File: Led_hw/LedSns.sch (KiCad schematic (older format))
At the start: 10 parts, among them Q1 TSOP48xx

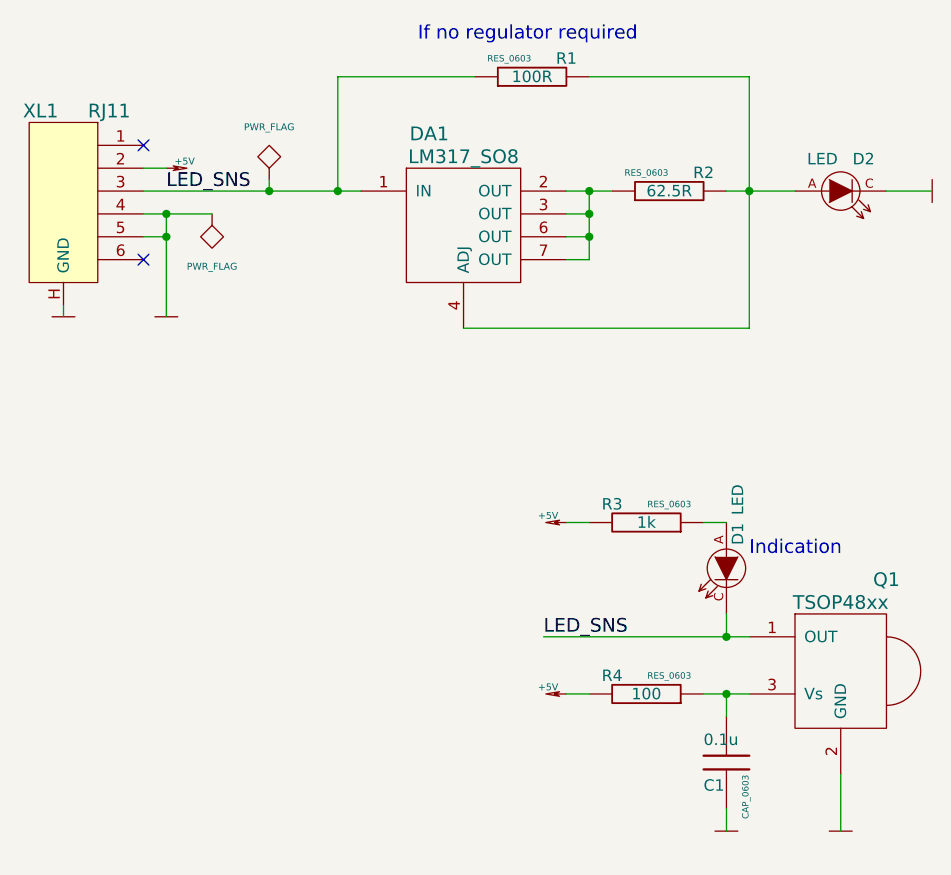
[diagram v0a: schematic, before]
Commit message: + LedSNS completed PCBs sent to production
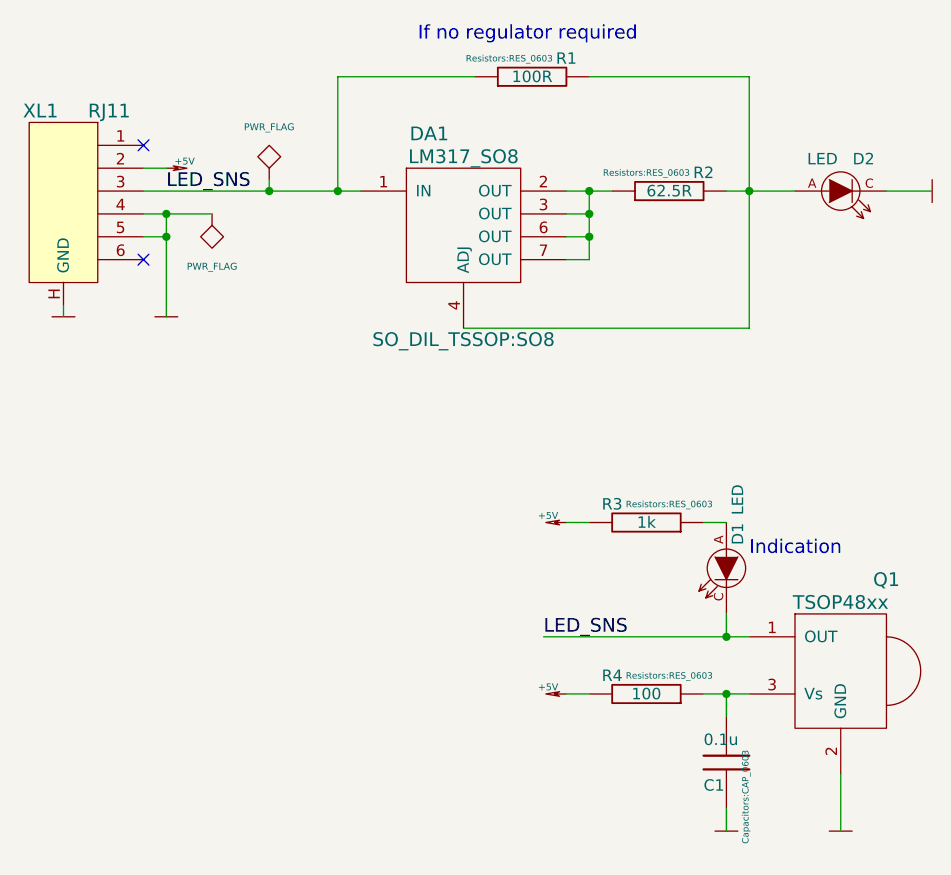
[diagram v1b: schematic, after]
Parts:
- C1: footprint CAP_0603 -> Capacitors:CAP_0603
- D1: footprint (none) -> LEDs:Through-Hole-3mm
- D2: footprint (none) -> LEDs:Through-Hole-5mm
- DA1: footprint ~ -> SO_DIL_TSSOP:SO8
- Q1: footprint (none) -> Sensors:TSOP48xx
- R1, R2, R3, R4: footprint RES_0603 -> Resistors:RES_0603
- XL1: footprint (none) -> Connectors:RJ11_TJ6_6P6C
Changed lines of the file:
@@
 F 0 "DA1" H 4150 2600 60  0000 C CNN
 F 1 "LM317_SO8" H 4300 2500 60  0000 C CNN
-F 2 "~" H 4300 2200 60  0000 C CNN
+F 2 "SO_DIL_TSSOP:SO8" H 4300 1700 60  0000 C CNN
 F 3 "~" H 4300 2200 60  0000 C CNN
 	1    4300 2200
@@
 F 0 "R2" V 5280 1900 50  0000 C CNN
 F 1 "62.5R" V 5200 2050 50  0000 C CNN
-F 2 "RES_0603" V 5280 2150 28  0000 C CNN
+F 2 "Resistors:RES_0603" V 5280 2150 28  0000 C CNN
 F 3 "~" H 5200 2050 60  0000 C CNN
 	1    5200 2050
@@
 F 0 "R1" V 4680 1400 50  0000 C CNN
 F 1 "100R" V 4600 1550 50  0000 C CNN
-F 2 "RES_0603" V 4680 1650 28  0000 C CNN
+F 2 "Resistors:RES_0603" V 4680 1650 28  0000 C CNN
 F 3 "~" H 4600 1550 60  0000 C CNN
 	1    4600 1550
@@
 F 0 "D2" H 6050 2190 50  0000 C CNN
 F 1 "LED" H 5870 2190 50  0000 C CNN
-F 2 "" H 5950 2050 60  0000 C CNN
+F 2 "LEDs:Through-Hole-5mm" H 5950 2050 60  0001 C CNN
 F 3 "" H 5950 2050 60  0000 C CNN
 	1    5950 2050
@@
 F 0 "XL1" H 2450 2500 60  0000 C CNN
 F 1 "RJ11" H 2750 2500 60  0000 C CNN
-F 2 "" H 2550 2100 60  0001 C CNN
+F 2 "Connectors:RJ11_TJ6_6P6C" H 2550 2100 60  0001 C CNN
 F 3 "" H 2550 2100 60  0001 C CNN
 	1    2550 2100
@@
 F 0 "Q1" H 5750 4450 60  0000 C CNN
 F 1 "TSOP48xx" H 5950 4350 60  0000 C CNN
-F 2 "" H 5950 4100 60  0000 C CNN
+F 2 "Sensors:TSOP48xx" H 5950 4100 60  0001 C CNN
 F 3 "" H 5950 4100 60  0000 C CNN
 	1    5950 4100
@@
 F 0 "R4" V 5180 4100 50  0000 C CNN
 F 1 "100" V 5100 4250 50  0000 C CNN
-F 2 "RES_0603" V 5180 4350 28  0000 C CNN
+F 2 "Resistors:RES_0603" V 5180 4350 28  0000 C CNN
 F 3 "" H 5100 4250 60  0000 C CNN
 	1    5100 4250
@@
 F 0 "C1" H 5350 4450 50  0000 L CNN
 F 1 "0.1u" H 5350 4650 50  0000 L CNN
-F 2 "CAP_0603" V 5550 4400 28  0000 C BNN
+F 2 "Capacitors:CAP_0603" V 5550 4400 28  0000 C BNN
 F 3 "" H 5450 4550 60  0000 C CNN
 	1    5450 4550
@@
 F 0 "D1" H 5300 3750 50  0000 C CNN
 F 1 "LED" H 5150 3750 50  0000 C CNN
-F 2 "" H 5450 3700 60  0000 C CNN
+F 2 "LEDs:Through-Hole-3mm" H 5450 3700 60  0001 C CNN
 F 3 "" H 5450 3700 60  0000 C CNN
 	1    5450 3700
@@
 F 0 "R3" V 5180 3350 50  0000 C CNN
 F 1 "1k" V 5100 3500 50  0000 C CNN
-F 2 "RES_0603" V 5180 3600 28  0000 C CNN
+F 2 "Resistors:RES_0603" V 5180 3600 28  0000 C CNN
 F 3 "" H 5100 3500 60  0000 C CNN
 	1    5100 3500
